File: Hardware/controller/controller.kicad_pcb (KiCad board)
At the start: 4 copper layers, 179 x 178 mm, 112 parts, among them J101 Conn_02x10_Odd_Even, J102 Conn_02x10_Odd_Even, J103 Conn_02x10_Odd_Even, J104 Conn_02x08_Odd_Even, J201 Screw_Terminal_01x03, J301 Conn_ARM_JTAG_SWD_10, M101 Fan_4pin, Q101 MMBT3904, Q301 MMBT3904, SW302 B3F-1002, U101 PCA9543A, U102 EMC2101-R, U302 ATSAME51J20A-A, U303 AT25SF321B-SSHB, U401 KSZ8041TL, X401 50MHz, Y302 12MHz

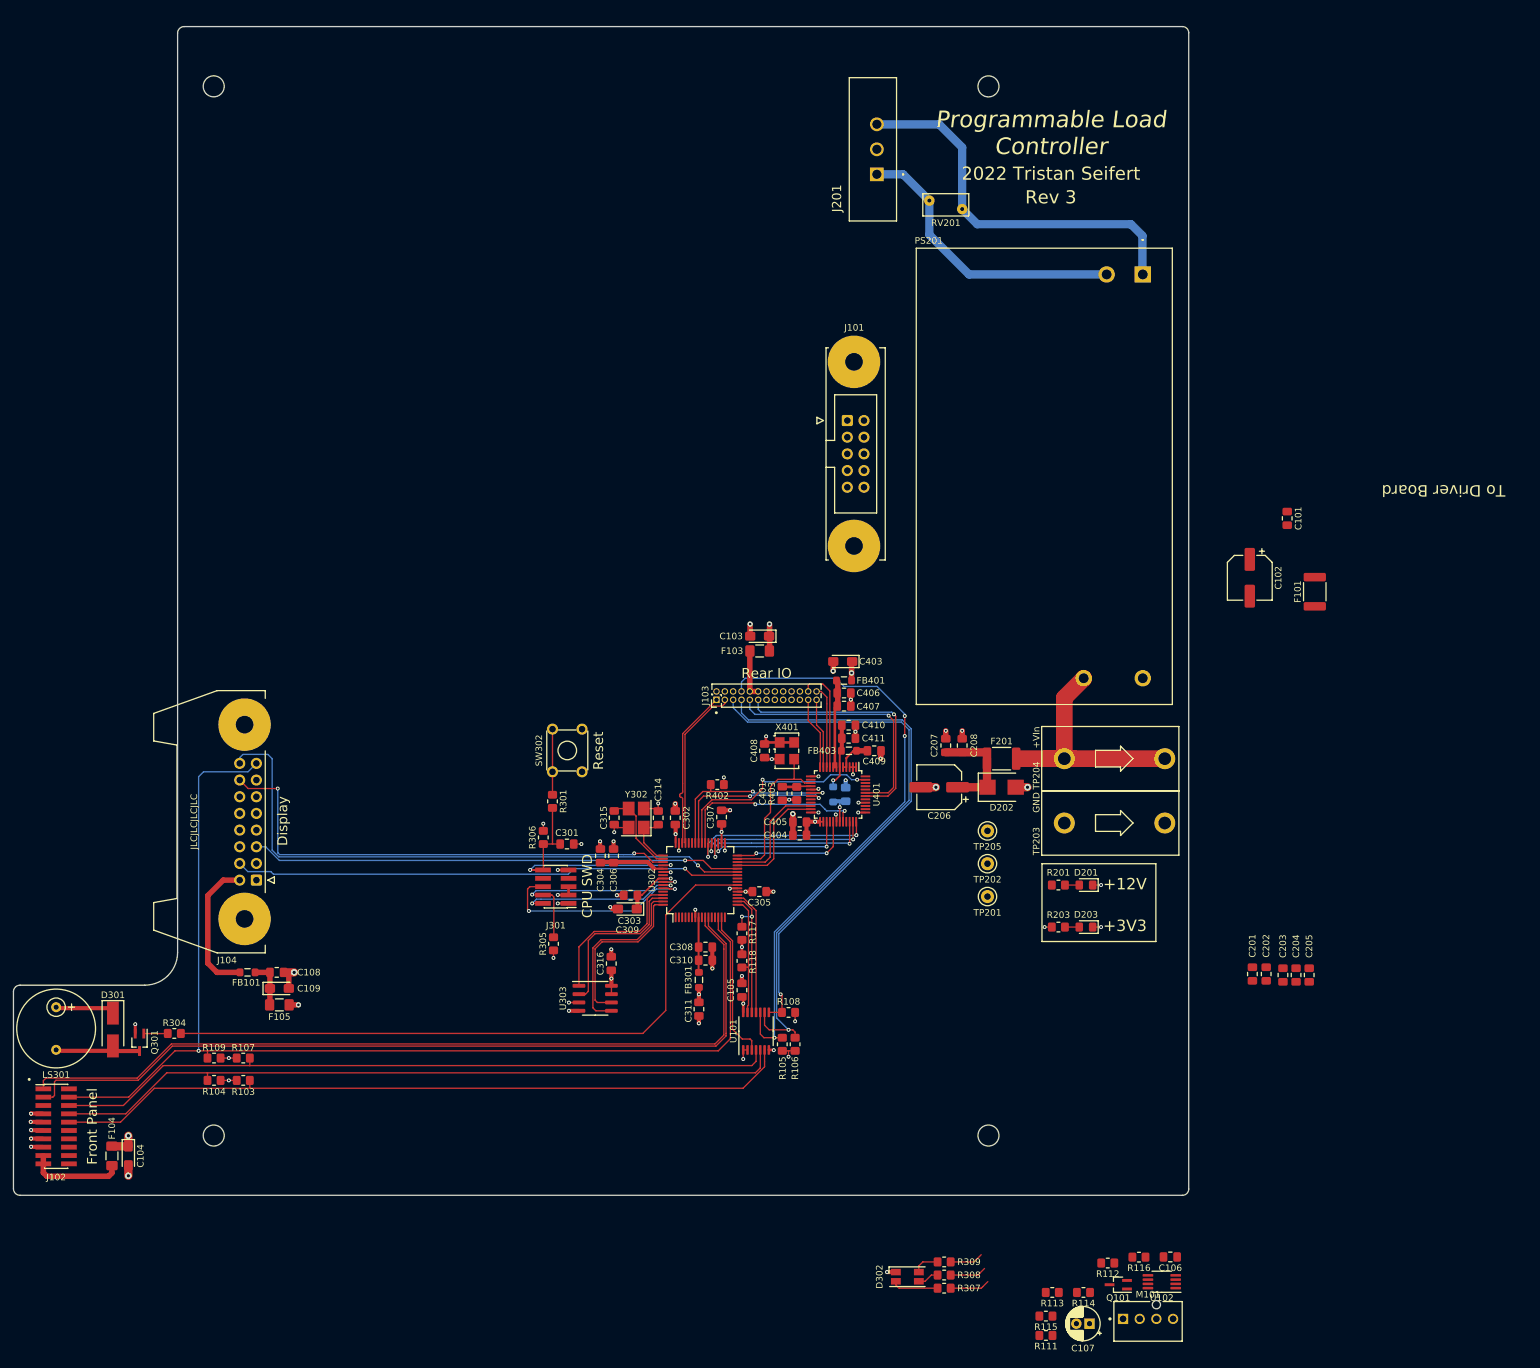
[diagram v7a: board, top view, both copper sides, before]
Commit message: More new layout stuff
- More work on the new controller board layout

- Rework rear IO board for the new Technomet rear panel (it has an
  expansion connector for CAN also, and features four screw holes
  instead of two)

- Added a few footprints (expansion RJ45 connector; some
  horizontal/vertical headers)
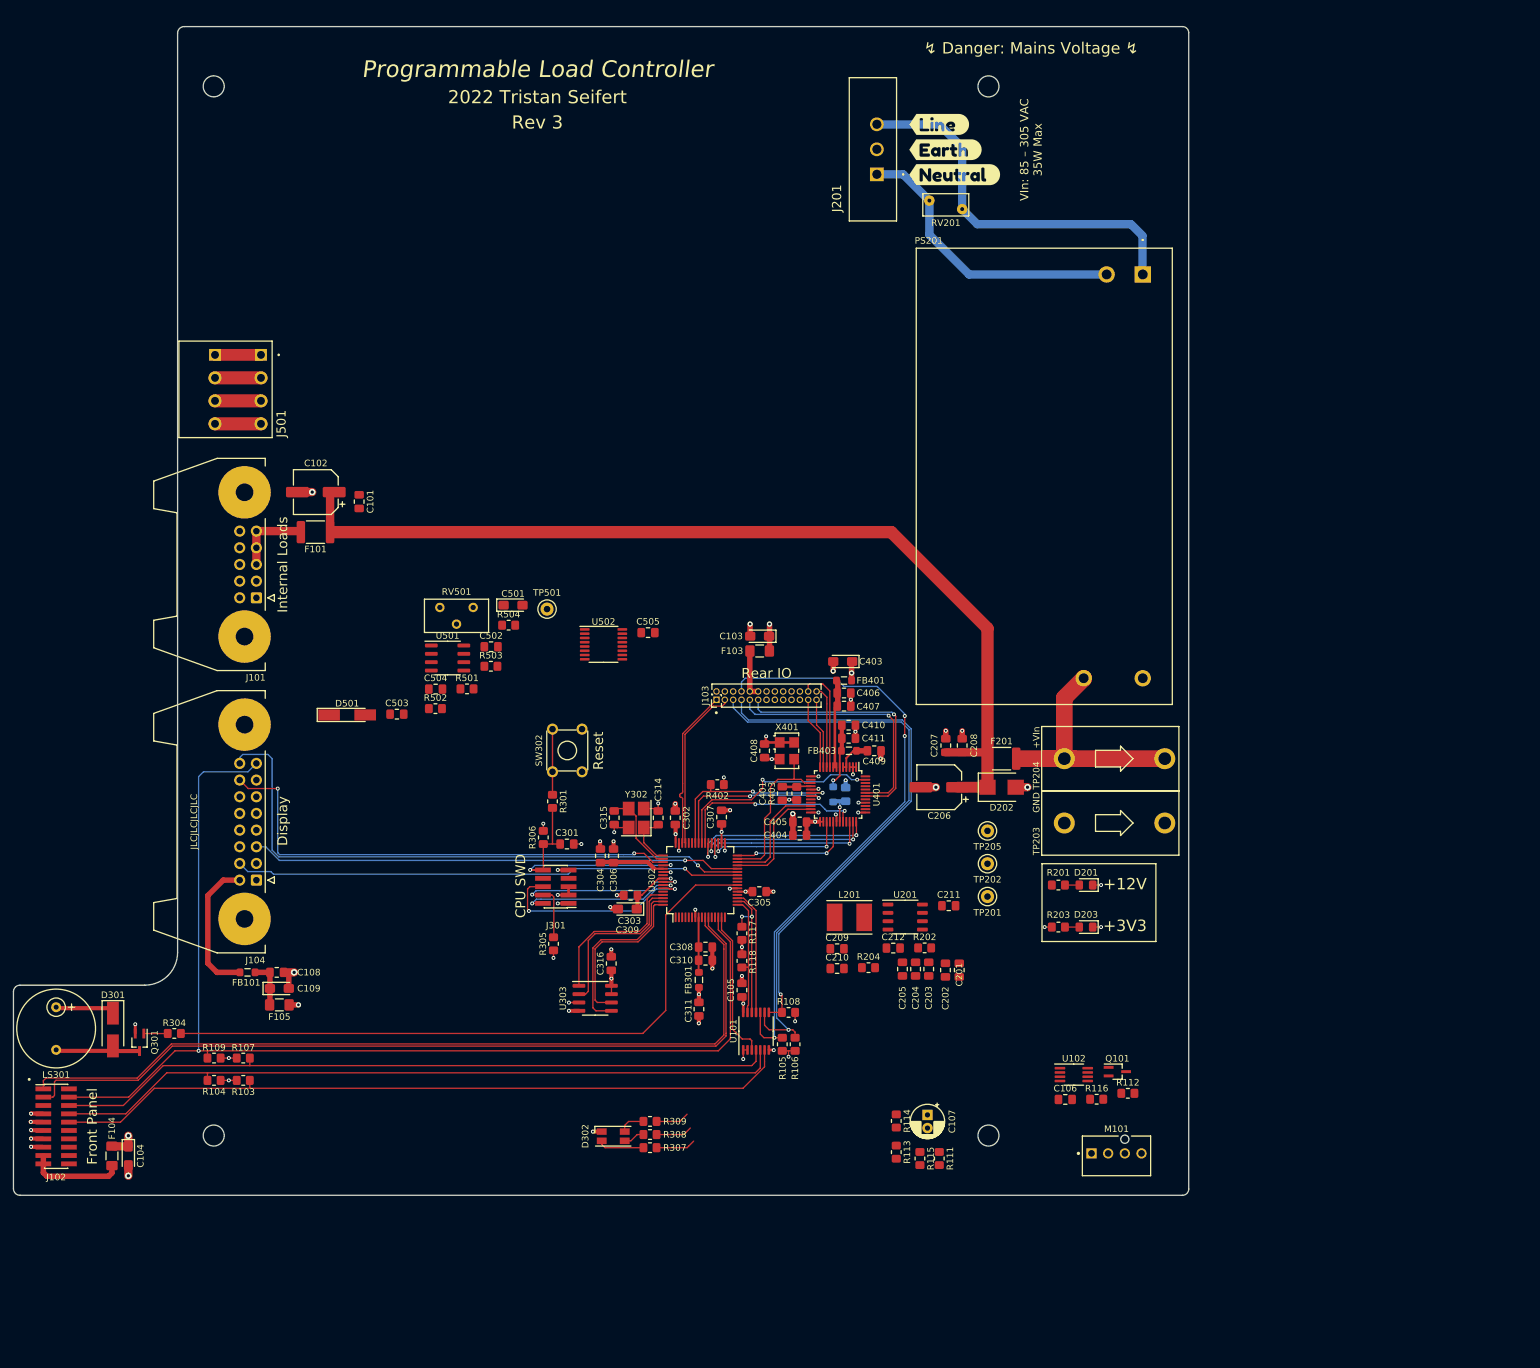
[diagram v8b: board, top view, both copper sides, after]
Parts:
- added C209: 10µF, Capacitor_SMD:C_0805_2012Metric_Pad1.18x1.45mm_HandSolder, F.Cu at (145.4, 162.4)
- added C210: 10nF, Capacitor_SMD:C_0805_2012Metric_Pad1.18x1.45mm_HandSolder, F.Cu at (145.4, 165.5)
- added C211: 1µF, Capacitor_SMD:C_0805_2012Metric_Pad1.18x1.45mm_HandSolder, F.Cu at (162.4, 155.9)
- added C212: 100nF, Capacitor_SMD:C_0805_2012Metric_Pad1.18x1.45mm_HandSolder, F.Cu at (154.0, 162.3)
- added C501: 10µF, Capacitor_Tantalum_SMD:CP_EIA-3216-18_Kemet-A_Pad1.58x1.35mm_HandSolder, F.Cu at (96.1, 110.1)
- added C502: 100nF, Capacitor_SMD:C_0805_2012Metric_Pad1.18x1.45mm_HandSolder, F.Cu at (92.8, 116.5)
- added C503: 100nF, Capacitor_SMD:C_0805_2012Metric_Pad1.18x1.45mm_HandSolder, F.Cu at (78.4, 126.7)
- added C504: 100nF, Capacitor_SMD:C_0805_2012Metric_Pad1.18x1.45mm_HandSolder, F.Cu at (84.3, 122.9)
- added C505: 100nF, Capacitor_SMD:C_0805_2012Metric_Pad1.18x1.45mm_HandSolder, F.Cu at (116.7, 114.3)
- added D501: 2V4, Diode_SMD:D_MiniMELF_Handsoldering, F.Cu at (70.8, 126.8)
- added J501: Conn_01x04, programmable-load:CUI_TBLH10-350-04BK, F.Cu at (57.7, 72.0)
- added L201: 2.2µH, Inductor_SMD:L_Taiyo-Yuden_NR-50xx_HandSoldering, F.Cu at (147.3, 157.7)
- added R202: 75k, Resistor_SMD:R_0805_2012Metric_Pad1.20x1.40mm_HandSolder, F.Cu at (158.8, 162.3)
- added R204: 22k, Resistor_SMD:R_0805_2012Metric_Pad1.20x1.40mm_HandSolder, F.Cu at (150.2, 165.3)
- added R501: 1M .1%, Resistor_SMD:R_0805_2012Metric_Pad1.20x1.40mm_HandSolder, F.Cu at (89.1, 122.9)
- added R502: 1M .1%, Resistor_SMD:R_0805_2012Metric_Pad1.20x1.40mm_HandSolder, F.Cu at (84.3, 125.9)
- added R503: 20k .1%, Resistor_SMD:R_0805_2012Metric_Pad1.20x1.40mm_HandSolder, F.Cu at (92.7, 119.4)
- added R504: 20k .1%, Resistor_SMD:R_0805_2012Metric_Pad1.20x1.40mm_HandSolder, F.Cu at (95.4, 113.2)
- added RV501: 20k, programmable-load:Potentiometer_Nidec_Copal_CT94EY, F.Cu at (90.0, 110.5)
- added TP501: VSense+, TestPoint:TestPoint_Keystone_5000-5004_Miniature, F.Cu at (101.3, 110.7)
- added U201: BD9D321EFJ, Package_SO:SOP-8_3.9x4.9mm_P1.27mm, F.Cu at (155.8, 157.6)
- added U501: OPA277, Package_SO:SOIC-8_3.9x4.9mm_P1.27mm, F.Cu at (86.1, 118.2)
- added U502: XRA1200, Package_SO:TSSOP-16_4.4x5mm_P0.65mm, F.Cu at (109.9, 116.1)
- added kibuzzard-6264DD48: G***, kibuzzard-6264DD48, F.Cu at (161.0, 36.9)
- added kibuzzard-6264DD56: G***, kibuzzard-6264DD56, F.Cu at (161.9, 40.8)
- added kibuzzard-6264DD70: G***, kibuzzard-6264DD70, F.Cu at (163.3, 44.5)
- J101: footprint Connector_IDC:IDC-Header_2x05-1MP_P2.54mm_Latch_Vertical -> Connector_IDC:IDC-Header_2x05-1MP_P2.54mm_Latch_Horizontal
- moved F101 152.5 mm to (66.0, 99.0), turned to 0 degrees
- moved C102 142.8 mm to (66.0, 92.9), turned to 180 degrees
- moved C101 141.4 mm to (72.7, 94.3)
- moved J101 94.0 mm to (57.0, 109.0), turned to 180 degrees
- moved C205 62.0 mm to (155.4, 165.6), turned to -90 degrees
- moved C204 58.0 mm to (157.4, 165.6), turned to -90 degrees
- moved C203 54.0 mm to (159.4, 165.6), turned to -90 degrees
- moved D302 49.6 mm to (111.3, 191.0)
- moved R307 49.6 mm to (117.0, 192.8)
- moved R308 49.6 mm to (117.0, 190.8)
- moved R309 49.6 mm to (117.0, 188.8)
- moved C202 48.9 mm to (161.9, 165.7), turned to 90 degrees
- moved C201 44.7 mm to (164.1, 165.7), turned to 90 degrees
- moved C107 40.2 mm to (159.2, 187.8), turned to -90 degrees
- moved R114 38.7 mm to (154.5, 188.7), turned to -90 degrees
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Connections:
- J101 pad 10: Net-(J101-Pad10) -> GND
- J101 pad 2: Net-(J101-Pad10) -> GND
- J101 pad 4: Net-(J101-Pad10) -> GND
- J101 pad 6: Net-(J101-Pad10) -> GND
- J101 pad 8: Net-(J101-Pad10) -> GND
- U302 pad 3: unconnected-(U302-Pad3) -> /VSENSE
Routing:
- net +12V: track 14.7 -> 146.0 mm
- net Net-(F101-Pad1): track 0.00 -> 11.7 mm
- net unconnected-(J501-Pad4): track 0.00 -> 7.00 mm
- net unconnected-(J501-Pad3): track 0.00 -> 7.00 mm
- net unconnected-(J501-Pad2): track 0.00 -> 7.00 mm
- net unconnected-(J501-Pad1): track 0.00 -> 7.00 mm
- net GND: track 86.9 -> 89.2 mm, vias 53 -> 54
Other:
- board text added: "Internal Loads"
- board text added: "VIn: 85 – 305 VAC 35W Max"
- board text added: "↯ Danger: Mains Voltage ↯"
- board text removed: "To Driver Board"
